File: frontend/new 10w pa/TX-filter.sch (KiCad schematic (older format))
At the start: 48 parts, among them K2 D3002, K3 D3002, K4 D3002, K5 D3002, K6 D3002, K7 D3002, U2 74LS145

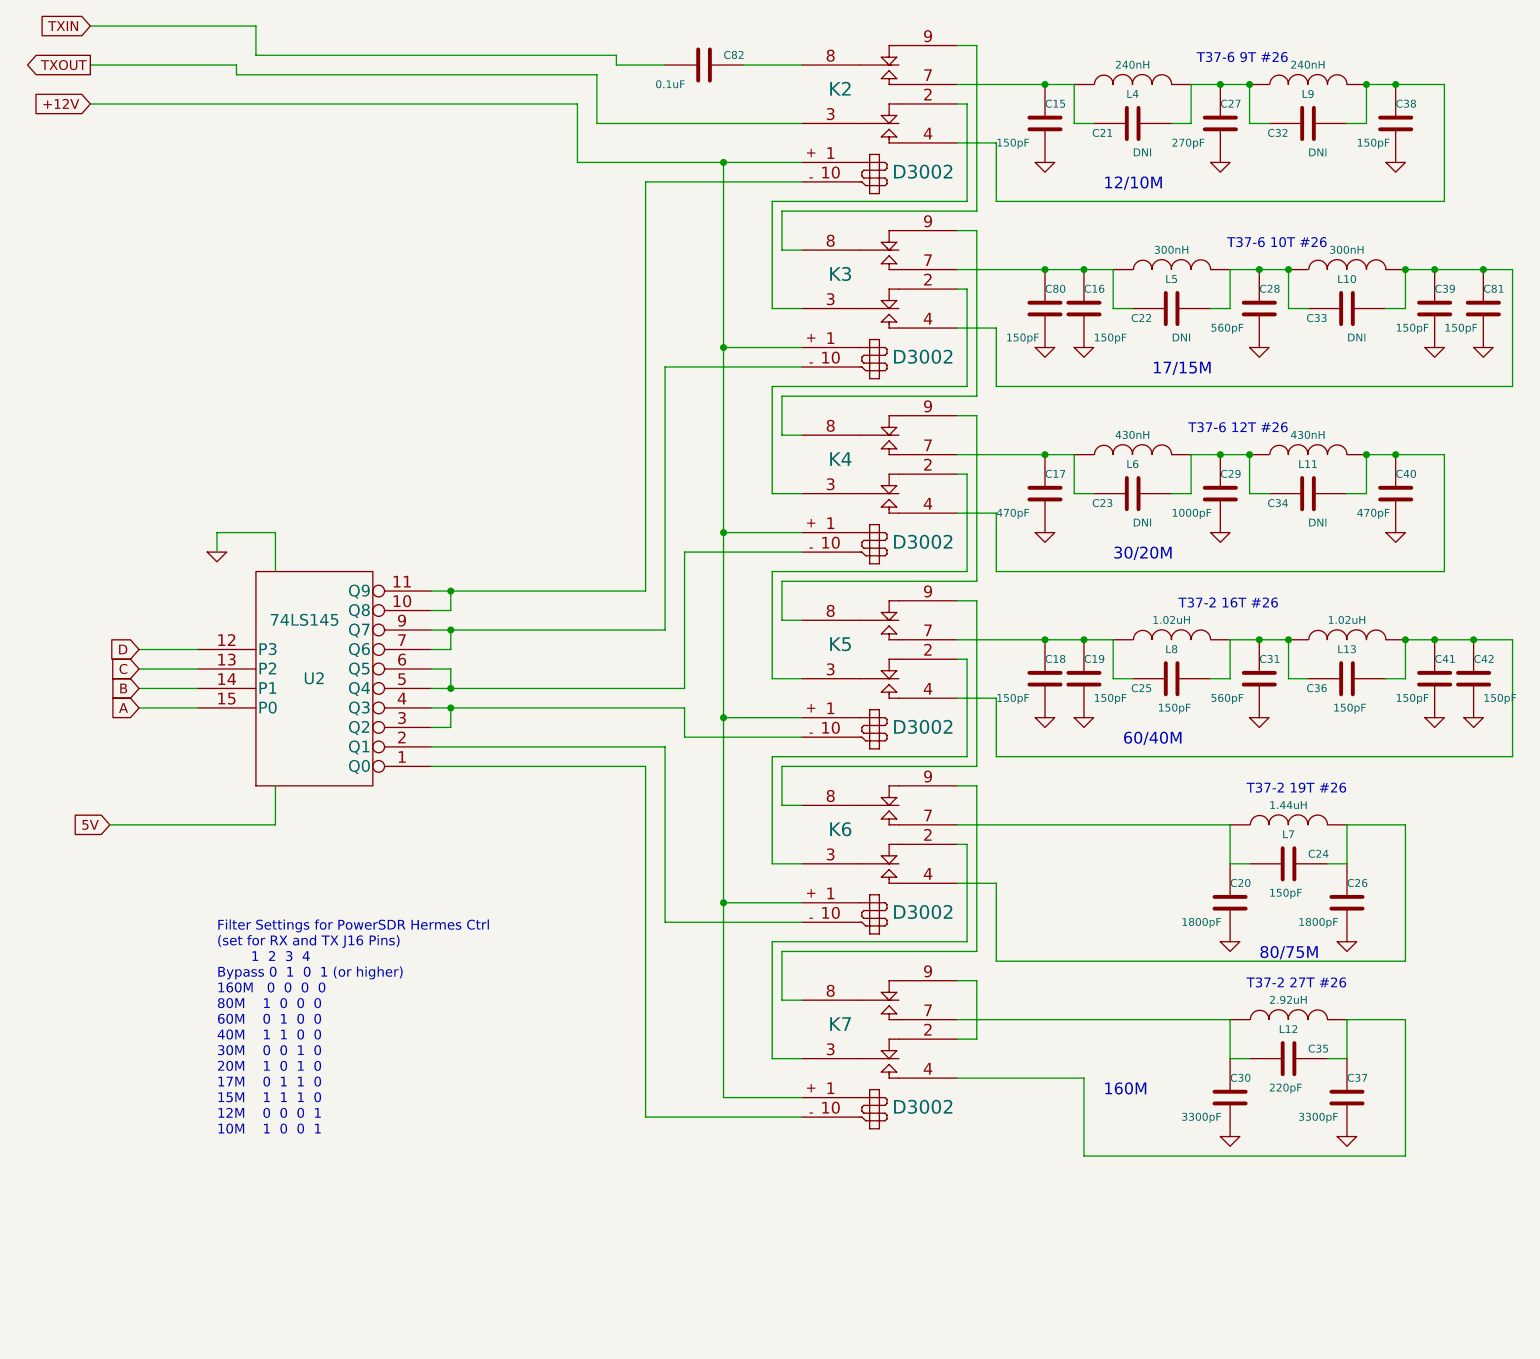
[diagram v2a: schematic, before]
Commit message: Added opto and change of PTT
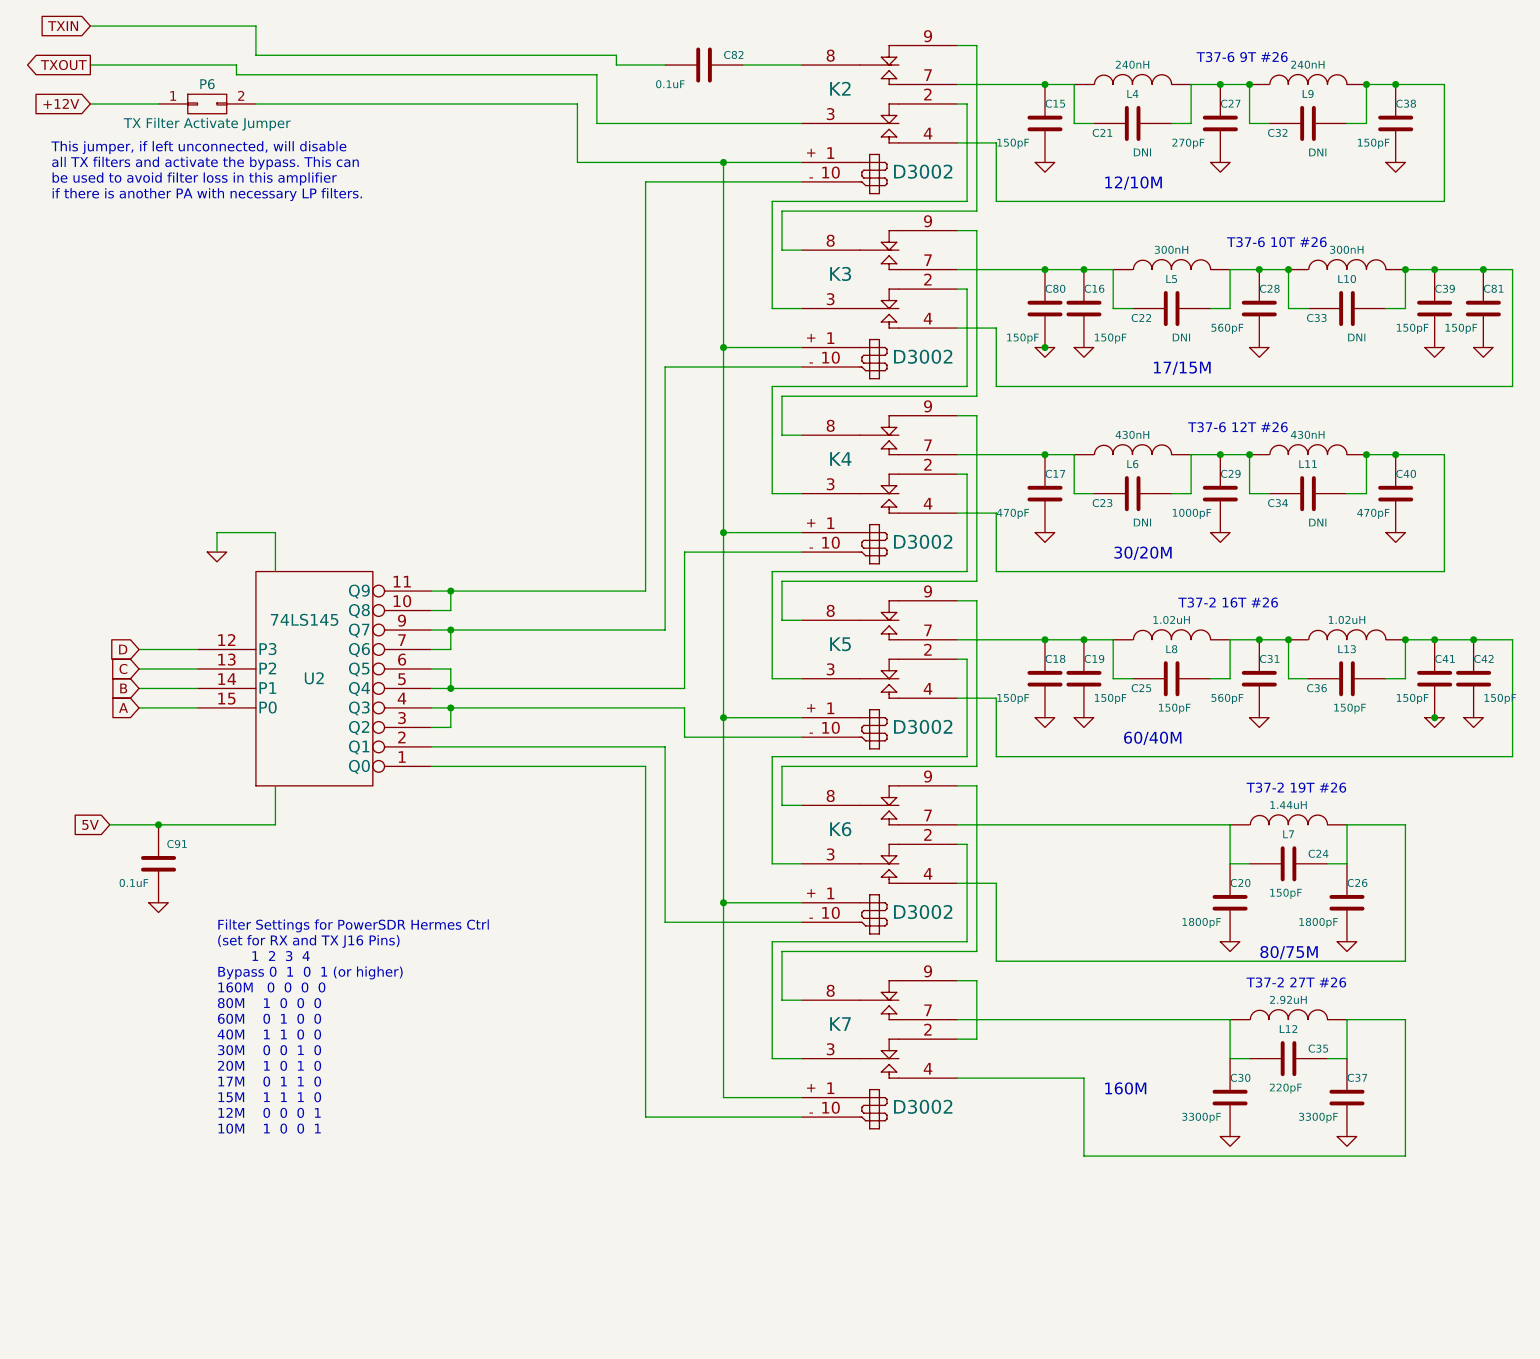
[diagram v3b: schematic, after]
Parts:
- added C91: 0.1uF, HERMESLITE:C_0805, symbol C
- added P6: TX Filter Activate Jumper, Pin_Headers:Pin_Header_Straight_1x02, symbol CONN_02X01
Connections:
- net +12V: now also P6.1 (P1); no longer K2.1 (+), K3.1 (+), K4.1 (+), K5.1 (+), K6.1 (+), K7.1 (+)
- net GND: now also C91.1
- net VCC: now also C91.2
- new net: K2.1 (+), K3.1 (+), K4.1 (+), K5.1 (+), K6.1 (+), K7.1 (+), P6.2 (P2)
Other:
- note added: "This jumper, if left unconnected, will disable\nall TX filters and activate the bypass. This can \nbe used to avoid filter loss in this amplifier \nif there is another PA with necessary LP filters. \n"
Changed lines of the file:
@@
 $EndComp
 $Comp
-L GND #PWR024
+L GND #PWR030
 U 1 1 5496A449
 P 6850 4150
-F 0 "#PWR024" H 6850 4150 30  0001 C CNN
+F 0 "#PWR030" H 6850 4150 30  0001 C CNN
 F 1 "GND" H 6850 4080 30  0001 C CNN
 F 2 "" H 6850 4150 60  0000 C CNN
@@
 $EndComp
 $Comp
-L GND #PWR025
+L GND #PWR031
 U 1 1 5496A44A
 P 5750 4150
-F 0 "#PWR025" H 5750 4150 30  0001 C CNN
+F 0 "#PWR031" H 5750 4150 30  0001 C CNN
 F 1 "GND" H 5750 4080 30  0001 C CNN
 F 2 "" H 5750 4150 60  0000 C CNN
@@
 $EndComp
 $Comp
-L GND #PWR026
+L GND #PWR032
 U 1 1 5496A44B
 P 7750 4150
-F 0 "#PWR026" H 7750 4150 30  0001 C CNN
+F 0 "#PWR032" H 7750 4150 30  0001 C CNN
 F 1 "GND" H 7750 4080 30  0001 C CNN
 F 2 "" H 7750 4150 60  0000 C CNN
@@
 $EndComp
 $Comp
-L GND #PWR027
+L GND #PWR033
 U 1 1 54A155CF
 P 6700 6300
-F 0 "#PWR027" H 6700 6300 30  0001 C CNN
+F 0 "#PWR033" H 6700 6300 30  0001 C CNN
 F 1 "GND" H 6700 6230 30  0001 C CNN
 F 2 "" H 6700 6300 60  0000 C CNN
@@
 $EndComp
 $Comp
-L GND #PWR028
+L GND #PWR034
 U 1 1 54A1568D
 P 7300 6300
-F 0 "#PWR028" H 7300 6300 30  0001 C CNN
+F 0 "#PWR034" H 7300 6300 30  0001 C CNN
 F 1 "GND" H 7300 6230 30  0001 C CNN
 F 2 "" H 7300 6300 60  0000 C CNN
@@
 $EndComp
 $Comp
-L GND #PWR029
+L GND #PWR035
 U 1 1 54A171EB
 P 6700 5300
-F 0 "#PWR029" H 6700 5300 30  0001 C CNN
+F 0 "#PWR035" H 6700 5300 30  0001 C CNN
 F 1 "GND" H 6700 5230 30  0001 C CNN
 F 2 "" H 6700 5300 60  0000 C CNN
@@
 $EndComp
 $Comp
-L GND #PWR030
+L GND #PWR036
 U 1 1 54A171F1
 P 7300 5300
-F 0 "#PWR030" H 7300 5300 30  0001 C CNN
+F 0 "#PWR036" H 7300 5300 30  0001 C CNN
 F 1 "GND" H 7300 5230 30  0001 C CNN
 F 2 "" H 7300 5300 60  0000 C CNN
@@
 $EndComp
 $Comp
-L GND #PWR031
+L GND #PWR037
 U 1 1 54A1B96C
 P 6650 3200
-F 0 "#PWR031" H 6650 3200 30  0001 C CNN
+F 0 "#PWR037" H 6650 3200 30  0001 C CNN
 F 1 "GND" H 6650 3130 30  0001 C CNN
 F 2 "" H 6650 3200 60  0000 C CNN
@@
 $EndComp
 $Comp
-L GND #PWR032
+L GND #PWR038
 U 1 1 54A1B972
 P 5750 3200
-F 0 "#PWR032" H 5750 3200 30  0001 C CNN
+F 0 "#PWR038" H 5750 3200 30  0001 C CNN
 F 1 "GND" H 5750 3130 30  0001 C CNN
 F 2 "" H 5750 3200 60  0000 C CNN
@@
 $EndComp
 $Comp
-L GND #PWR033
+L GND #PWR039
 U 1 1 54A1B978
 P 7550 3200
-F 0 "#PWR033" H 7550 3200 30  0001 C CNN
+F 0 "#PWR039" H 7550 3200 30  0001 C CNN
 F 1 "GND" H 7550 3130 30  0001 C CNN
 F 2 "" H 7550 3200 60  0000 C CNN
@@
 $EndComp
 $Comp
-L GND #PWR034
+L GND #PWR040
 U 1 1 54A1CC1F
 P 6850 2250
-F 0 "#PWR034" H 6850 2250 30  0001 C CNN
+F 0 "#PWR040" H 6850 2250 30  0001 C CNN
 F 1 "GND" H 6850 2180 30  0001 C CNN
 F 2 "" H 6850 2250 60  0000 C CNN
@@
 $EndComp
 $Comp
-L GND #PWR035
+L GND #PWR041
 U 1 1 54A1CC25
 P 5950 2250
-F 0 "#PWR035" H 5950 2250 30  0001 C CNN
+F 0 "#PWR041" H 5950 2250 30  0001 C CNN
 F 1 "GND" H 5950 2180 30  0001 C CNN
 F 2 "" H 5950 2250 60  0000 C CNN
@@
 $EndComp
 $Comp
-L GND #PWR036
+L GND #PWR042
 U 1 1 54A1CC2B
 P 7750 2250
-F 0 "#PWR036" H 7750 2250 30  0001 C CNN
+F 0 "#PWR042" H 7750 2250 30  0001 C CNN
 F 1 "GND" H 7750 2180 30  0001 C CNN
 F 2 "" H 7750 2250 60  0000 C CNN
@@
 $EndComp
 $Comp
-L GND #PWR037
+L GND #PWR043
 U 1 1 54A1CDA5
 P 6650 1300
-F 0 "#PWR037" H 6650 1300 30  0001 C CNN
+F 0 "#PWR043" H 6650 1300 30  0001 C CNN
 F 1 "GND" H 6650 1230 30  0001 C CNN
 F 2 "" H 6650 1300 60  0000 C CNN
@@
 $EndComp
 $Comp
-L GND #PWR038
+L GND #PWR044
 U 1 1 54A1CDAB
 P 5750 1300
-F 0 "#PWR038" H 5750 1300 30  0001 C CNN
+F 0 "#PWR044" H 5750 1300 30  0001 C CNN
 F 1 "GND" H 5750 1230 30  0001 C CNN
 F 2 "" H 5750 1300 60  0000 C CNN
@@
 $EndComp
 $Comp
-L GND #PWR039
+L GND #PWR045
 U 1 1 54A1CDB1
 P 7550 1300
-F 0 "#PWR039" H 7550 1300 30  0001 C CNN
+F 0 "#PWR045" H 7550 1300 30  0001 C CNN
 F 1 "GND" H 7550 1230 30  0001 C CNN
 F 2 "" H 7550 1300 60  0000 C CNN
@@
 Wire Wire Line
 	1600 800  850  800
-Wire Wire Line
-	850  1000 3350 1000
 Text GLabel 950  4700 0    50   Input ~ 0
 5V
@@
 $EndComp
 $Comp
-L GND #PWR040
+L GND #PWR046
 U 1 1 54A63C22
 P 5950 4150
-F 0 "#PWR040" H 5950 4150 30  0001 C CNN
+F 0 "#PWR046" H 5950 4150 30  0001 C CNN
 F 1 "GND" H 5950 4080 30  0001 C CNN
 F 2 "" H 5950 4150 60  0000 C CNN
@@
 Connection ~ 7950 3750
 $Comp
-L GND #PWR041
+L GND #PWR047
 U 1 1 54A64006
 P 7950 4150
-F 0 "#PWR041" H 7950 4150 30  0001 C CNN
+F 0 "#PWR047" H 7950 4150 30  0001 C CNN
 F 1 "GND" H 7950 4080 30  0001 C CNN
 F 2 "" H 7950 4150 60  0000 C CNN
@@
 $EndComp
 $Comp
-L GND #PWR042
+L GND #PWR048
 U 1 1 54ABE5DE
 P 5750 2250
-F 0 "#PWR042" H 5750 2250 30  0001 C CNN
+F 0 "#PWR048" H 5750 2250 30  0001 C CNN
 F 1 "GND" H 5750 2180 30  0001 C CNN
 F 2 "" H 5750 2250 60  0000 C CNN
@@
 $EndComp
 $Comp
-L GND #PWR043
+L GND #PWR049
 U 1 1 54ABE6E0
 P 8000 2250
-F 0 "#PWR043" H 8000 2250 30  0001 C CNN
+F 0 "#PWR049" H 8000 2250 30  0001 C CNN
 F 1 "GND" H 8000 2180 30  0001 C CNN
 F 2 "" H 8000 2250 60  0000 C CNN
@@
 	1800 4500 1800 4700
 $Comp
-L GND #PWR044
+L GND #PWR050
 U 1 1 54C17C04
 P 1500 3300
-F 0 "#PWR044" H 1500 3300 30  0001 C CNN
+F 0 "#PWR050" H 1500 3300 30  0001 C CNN
 F 1 "GND" H 1500 3230 30  0001 C CNN
 F 2 "" H 1500 3300 60  0000 C CNN
@@
 Wire Wire Line
 	1100 3800 1400 3800
+Connection ~ 7750 4150
+Connection ~ 5750 2250
+$Comp
+L CONN_02X01 P6
+U 1 1 54D66FF2
+P 1450 1000
+F 0 "P6" H 1450 1100 50  0000 C CNN
+F 1 "TX Filter Activate Jumper" H 1450 900 50  0000 C CNN
+F 2 "Pin_Headers:Pin_Header_Straight_1x02" H 1450 -200 60  0001 C CNN
+F 3 "" H 1450 -200 60  0000 C CNN
+	1    1450 1000
+	1    0    0    -1
+$EndComp
+Wire Wire Line
+	1200 1000 850  1000
+Wire Wire Line
+	1700 1000 3350 1000
+Text Notes 650  1500 0    50   ~ 0
+This jumper, if left unconnected, will disable\nall TX filters and activate the bypass. This can \nbe used to avoid filter loss in this amplifier \nif there is another PA with necessary LP filters. \n
+$Comp
+L C C91
+U 1 1 54D8E8FD
+P 1200 4900
+F 0 "C91" H 1050 4800 40  0000 L CNN
+F 1 "0.1uF" H 1250 5000 40  0000 L CNN
+F 2 "HERMESLITE:C_0805" H 1238 4750 30  0001 C CNN
+F 3 "" H 1200 4900 60  0000 C CNN
+	1    1200 4900
+	-1   0    0    1
+$EndComp
+Connection ~ 1200 4700
+$Comp
+L GND #PWR051
+U 1 1 54D8EEE9
+P 1200 5100
+F 0 "#PWR051" H 1200 5100 30  0001 C CNN
+F 1 "GND" H 1200 5030 30  0001 C CNN
+F 2 "" H 1200 5100 60  0000 C CNN
+F 3 "" H 1200 5100 60  0000 C CNN
+	1    1200 5100
+	1    0    0    -1
+$EndComp
 $EndSCHEMATC
